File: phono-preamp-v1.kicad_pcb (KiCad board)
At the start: 2 copper layers, 57 x 32.5 mm, 43 parts, among them J1 Screw_Terminal_01x02, J2 Screw_Terminal_01x03, J3 Screw_Terminal_01x02, U1 NE5534, U2 NE5534

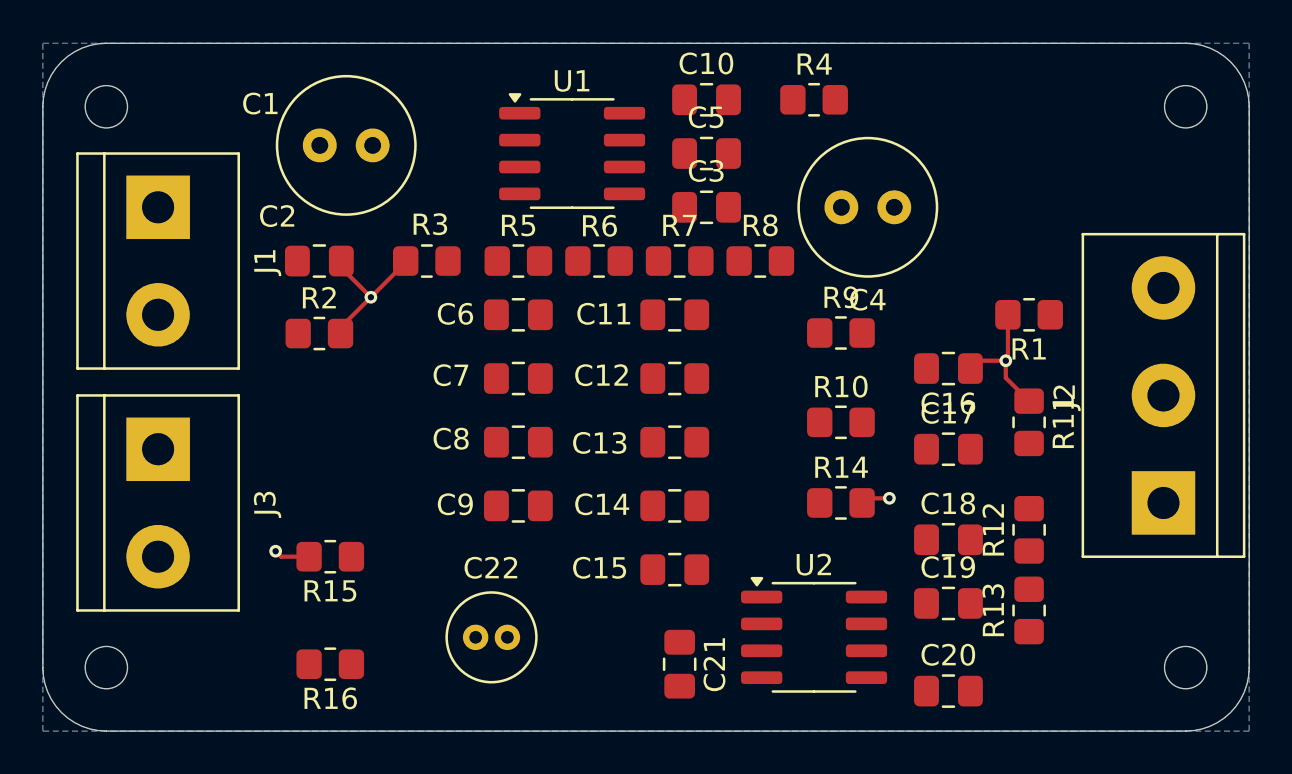
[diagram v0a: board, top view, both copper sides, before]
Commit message: Run critical power traces
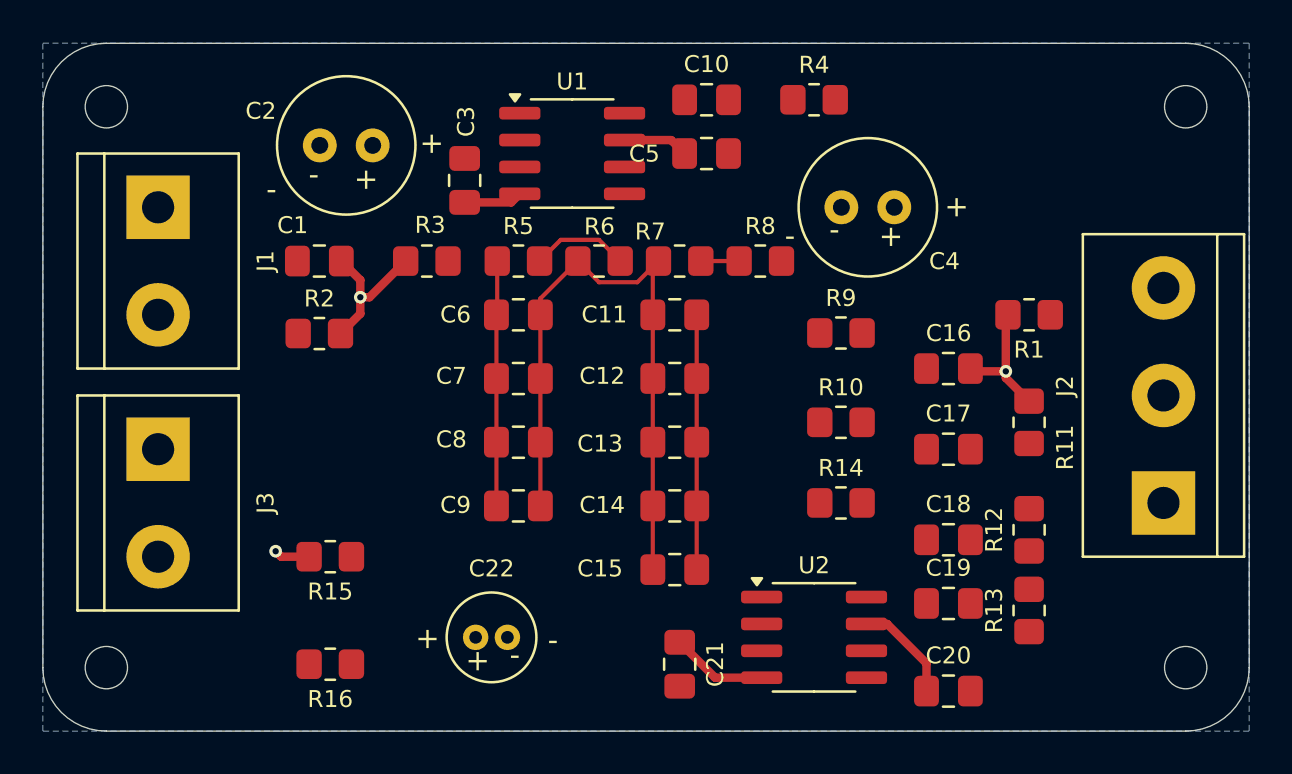
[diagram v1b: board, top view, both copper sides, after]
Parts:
- moved C3 11.5 mm to (138.4, 94.0), turned to -90 degrees
- turned C5 to 180 degrees
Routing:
- net Net-(C11-Pad1): track 0.00 -> 31.6 mm
- net Net-(C11-Pad2): track 0.00 -> 12.0 mm
- net Net-(U1--): track 0.00 -> 11.6 mm
- net +15V: track 0.00 -> 8.02 mm
- net -15V: track 0.00 -> 7.34 mm
- net Net-(R5-Pad2): track 0.00 -> 4.64 mm
- net Net-(R7-Pad2): track 0.00 -> 1.81 mm
- net GNDS: track 16.5 -> 15.0 mm, vias 4 -> 3
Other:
- board text added: "+"
- board text added: "-"

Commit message: Complete routing; shrink board size
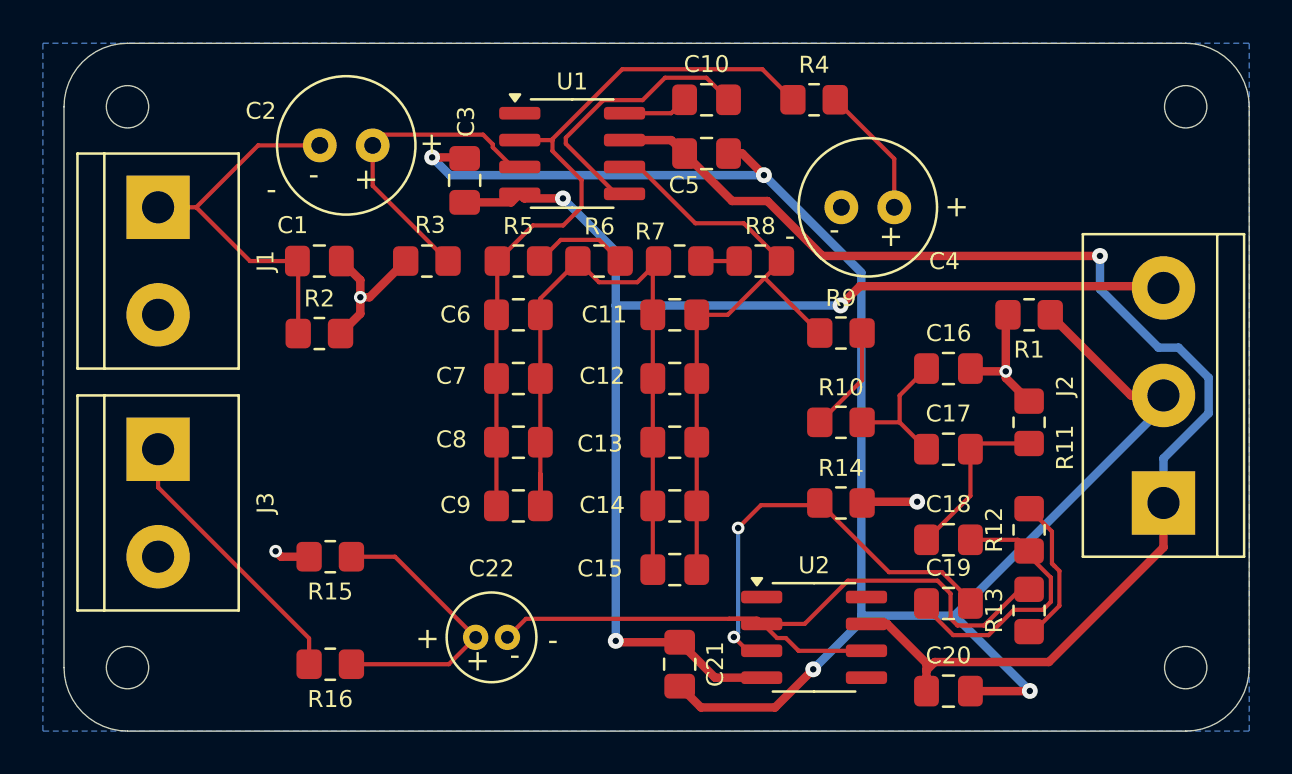
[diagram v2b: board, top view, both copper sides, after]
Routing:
- net 0: track 0.00 -> 87.0 mm, vias 0 -> 4
- net +15V: track 8.02 -> 61.4 mm, vias 0 -> 1
- net -15V: track 7.34 -> 60.7 mm, vias 0 -> 3
- net Net-(U2--): track 0.00 -> 35.4 mm
- net Net-(U1--): track 11.6 -> 35.3 mm
- net Net-(U2-+): track 0.00 -> 20.4 mm, vias 0 -> 2
- net /in: track 0.00 -> 18.1 mm
- net Net-(C11-Pad2): track 12.0 -> 30.0 mm
- net Net-(U1-+): track 0.00 -> 14.8 mm
- net Net-(C22-Pad1): track 0.00 -> 13.8 mm
- net Net-(U1-COMP): track 0.00 -> 13.3 mm
- net /out: track 0.00 -> 13.1 mm
- net Net-(C18-Pad2): track 0.00 -> 13.1 mm
- net Net-(C17-Pad2): track 0.00 -> 8.02 mm
- net Net-(R12-Pad2): track 0.00 -> 7.29 mm
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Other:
- board size 57 x 32.5 mm -> 56 x 32.5 mm
